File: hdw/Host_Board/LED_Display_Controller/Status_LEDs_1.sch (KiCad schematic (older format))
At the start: 5 parts

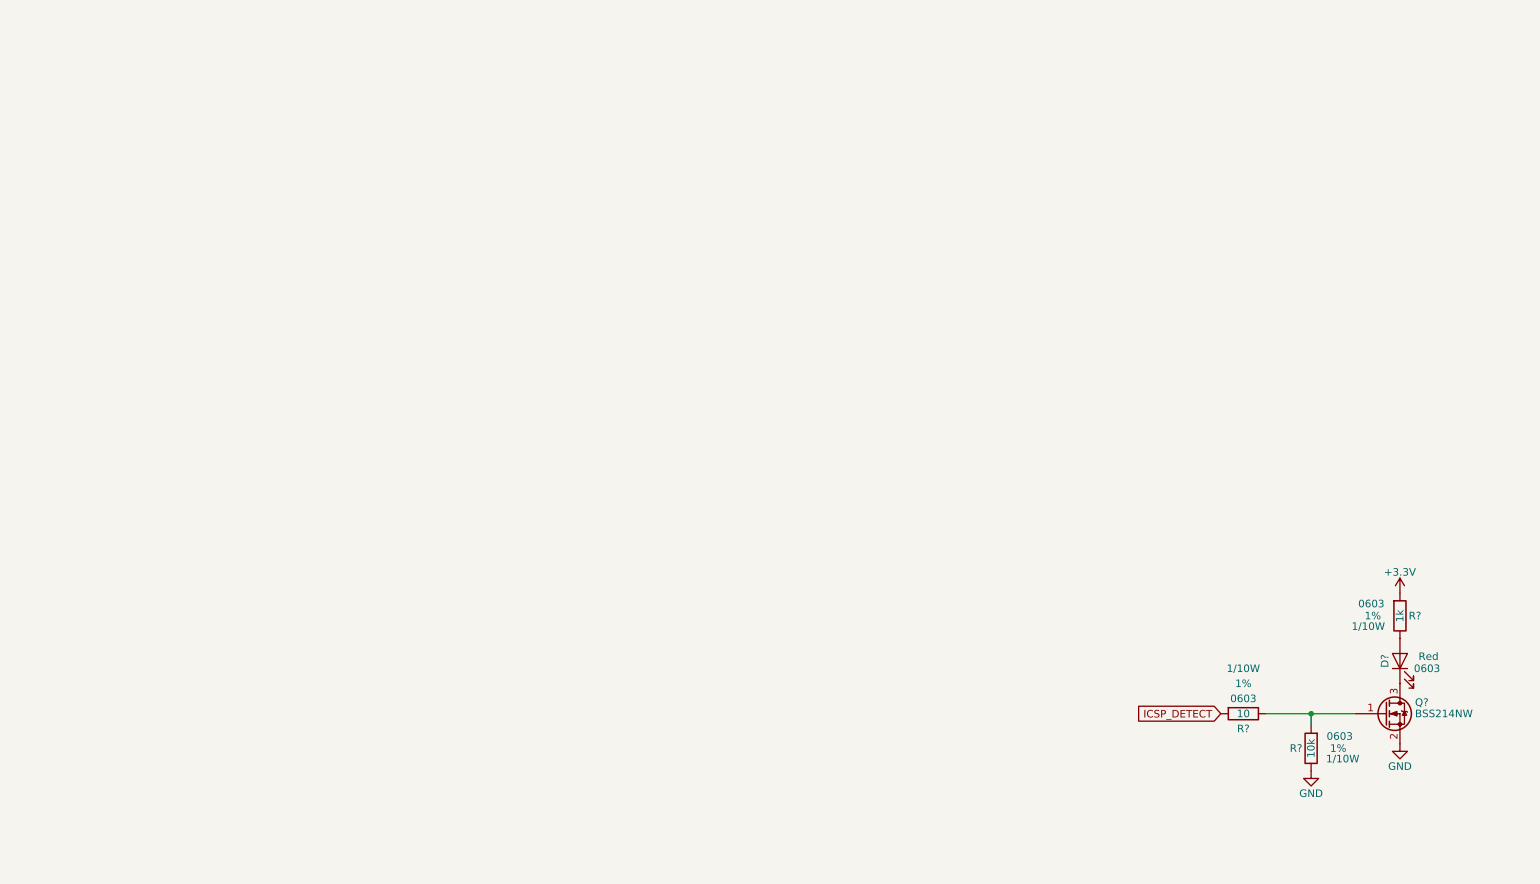
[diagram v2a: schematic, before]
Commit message: Converted to KiCad 5.0.1 project, resolved library issues, cleaned up a few sheets
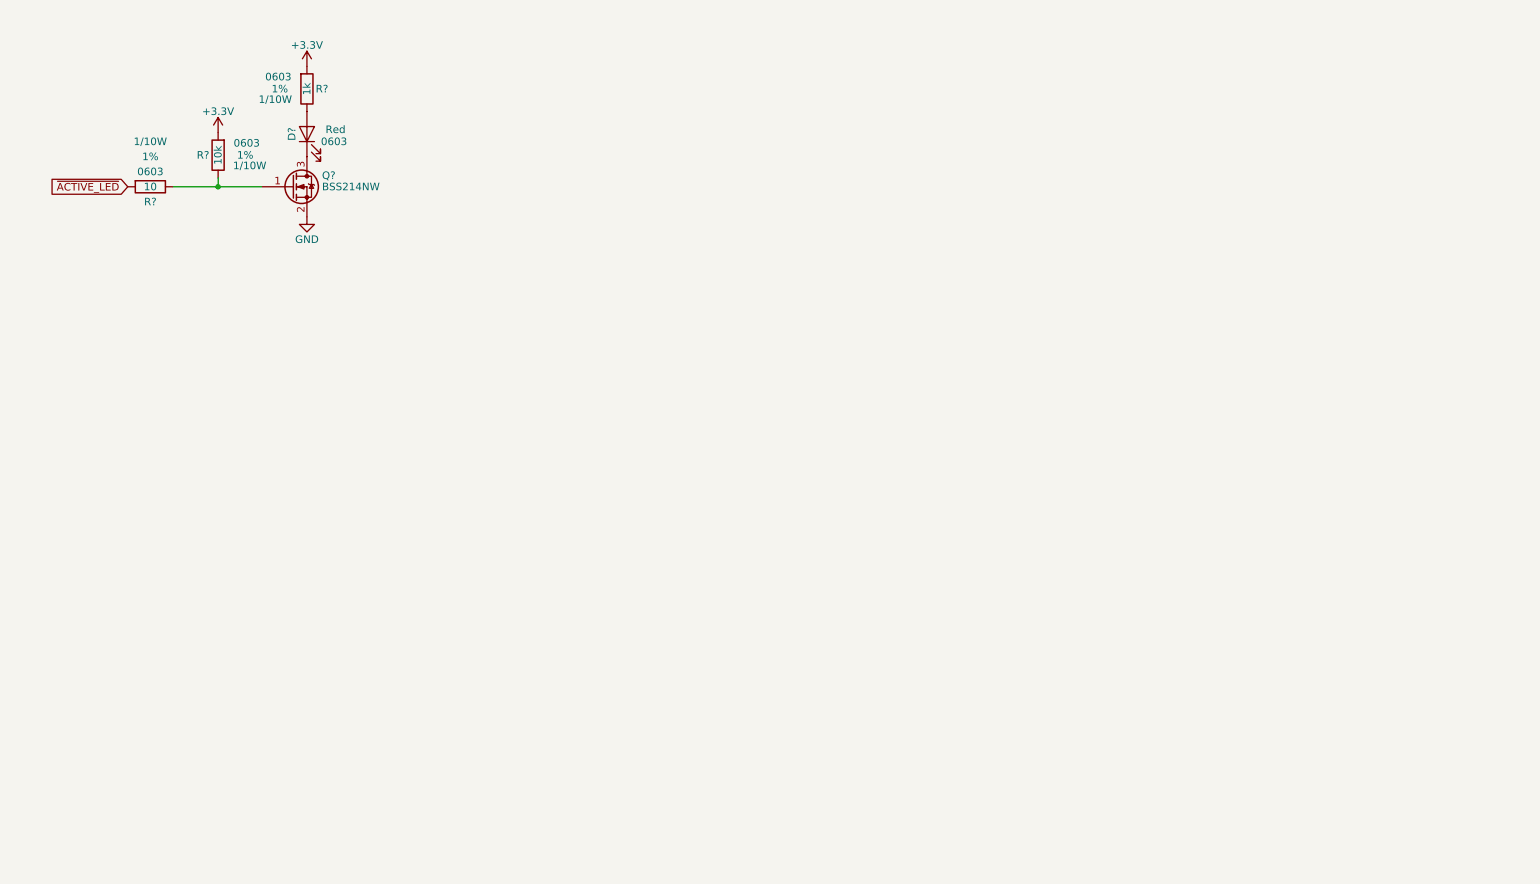
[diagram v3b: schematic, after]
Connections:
- net +3V3: now also R?.1
- net GND: no longer R?.2
- net at Q?.1 (G), R?.2: now also R?.2; no longer R?.1
- net ICSP_DETECT renamed ~ACTIVE_LED
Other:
- moved on the sheet: D?, Q?, R?
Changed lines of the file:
@@
 $Descr A 11000 8500
 encoding utf-8
-Sheet 22 25
+Sheet 21 25
 Title ""
 Date ""
@@
 L Transistor_FET:BSS214NW Q?
 U 1 1 5BC13AD2
-P 9500 5190
+P 2240 1690
 AR Path="/5BAAE16C/5BC13AD2" Ref="Q?"  Part="1"
 AR Path="/5BB844FD/5BC13AD2" Ref="Q?"  Part="1"
-F 0 "Q?" H 9700 5265 50  0000 L CNN
-F 1 "BSS214NW" H 9700 5190 50  0000 L CNN
-F 2 "Package_TO_SOT_SMD:SOT-323_SC-70" H 9700 5115 50  0001 L CIN
-F 3 "https://www.infineon.com/dgdl/Infineon-BSS214NW-DS-v02_02-en.pdf?fileId=db3a30431b3e89eb011b695aebc01bde" H 9500 5190 50  0001 L CNN
-	1    9500 5190
+F 0 "Q?" H 2440 1765 50  0000 L CNN
+F 1 "BSS214NW" H 2440 1690 50  0000 L CNN
+F 2 "Package_TO_SOT_SMD:SOT-323_SC-70" H 2440 1615 50  0001 L CIN
+F 3 "https://www.infineon.com/dgdl/Infineon-BSS214NW-DS-v02_02-en.pdf?fileId=db3a30431b3e89eb011b695aebc01bde" H 2240 1690 50  0001 L CNN
+	1    2240 1690
 	1    0    0    -1
 $EndComp
@@
 L power:GND #PWR?
 U 1 1 5BC13AD9
-P 9600 5390
-F 0 "#PWR?" H 9600 5140 50  0001 C CNN
-F 1 "GND" H 9600 5240 50  0000 C CNN
-F 2 "" H 9600 5390 50  0001 C CNN
-F 3 "" H 9600 5390 50  0001 C CNN
-	1    9600 5390
+P 2340 1890
+F 0 "#PWR?" H 2340 1640 50  0001 C CNN
+F 1 "GND" H 2340 1740 50  0000 C CNN
+F 2 "" H 2340 1890 50  0001 C CNN
+F 3 "" H 2340 1890 50  0001 C CNN
+	1    2340 1890
 	1    0    0    -1
 $EndComp
@@
 L Device:LED D?
 U 1 1 5BC13AE0
-P 9600 4840
-F 0 "D?" H 9600 4940 50  0000 C CNN
-F 1 "Red" V 9630 4650 50  0000 C CNN
-F 2 "" H 9600 4840 50  0001 C CNN
-F 3 "~" H 9600 4840 50  0001 C CNN
-F 4 "0603" V 9550 4660 50  0000 C CNN "foot"
-	1    9600 4840
+P 2340 1340
+F 0 "D?" H 2340 1440 50  0000 C CNN
+F 1 "Red" V 2370 1150 50  0000 C CNN
+F 2 "" H 2340 1340 50  0001 C CNN
+F 3 "~" H 2340 1340 50  0001 C CNN
+F 4 "0603" V 2290 1160 50  0000 C CNN "foot"
+	1    2340 1340
 	0    -1   -1   0
 $EndComp
@@
 L LED_Display_Local_Library:R_Custom R?
 U 1 1 5BC13AEB
-P 9600 4540
+P 2340 1040
 AR Path="/5BAAE1F3/5BC13AEB" Ref="R?"  Part="1"
 AR Path="/5BAAE1DC/5BC13AEB" Ref="R?"  Part="1"
 AR Path="/5BAAE16C/5BC13AEB" Ref="R?"  Part="1"
 AR Path="/5BB844FD/5BC13AEB" Ref="R?"  Part="1"
-F 0 "R?" H 9500 4540 50  0000 C CNN
-F 1 "1k" V 9600 4540 50  0000 C CNN
-F 2 "" H 9600 4540 50  0001 C CNN
-F 3 "" H 9600 4540 50  0001 C CNN
-F 4 "0603" H 9790 4620 50  0000 C CNN "display_footprint"
-F 5 "1%" H 9780 4540 50  0000 C CNN "Tolerance"
-F 6 "1/10W" H 9810 4470 50  0000 C CNN "Wattage"
-F 7 "PN" H 9900 4940 60  0001 C CNN "Digi-Key PN"
-	1    9600 4540
+F 0 "R?" H 2240 1040 50  0000 C CNN
+F 1 "1k" V 2340 1040 50  0000 C CNN
+F 2 "" H 2340 1040 50  0001 C CNN
+F 3 "" H 2340 1040 50  0001 C CNN
+F 4 "0603" H 2530 1120 50  0000 C CNN "display_footprint"
+F 5 "1%" H 2520 1040 50  0000 C CNN "Tolerance"
+F 6 "1/10W" H 2550 970 50  0000 C CNN "Wattage"
+F 7 "PN" H 2640 1440 60  0001 C CNN "Digi-Key PN"
+	1    2340 1040
 	-1   0    0    -1
 $EndComp
@@
 L LED_Display_Local_Library:R_Custom R?
 U 1 1 5BC13AF6
-P 8560 5190
-F 0 "R?" V 8460 5190 50  0000 C CNN
-F 1 "10" V 8560 5190 50  0000 C CNN
-F 2 "" H 8560 5190 50  0001 C CNN
-F 3 "" H 8560 5190 50  0001 C CNN
-F 4 "0603" V 8660 5190 50  0000 C CNN "display_footprint"
-F 5 "1%" V 8760 5190 50  0000 C CNN "Tolerance"
-F 6 "1/10W" V 8860 5190 50  0000 C CNN "Wattage"
-F 7 "PN" H 8860 5590 60  0001 C CNN "Digi-Key PN"
-	1    8560 5190
+P 1300 1690
+F 0 "R?" V 1200 1690 50  0000 C CNN
+F 1 "10" V 1300 1690 50  0000 C CNN
+F 2 "" H 1300 1690 50  0001 C CNN
+F 3 "" H 1300 1690 50  0001 C CNN
+F 4 "0603" V 1400 1690 50  0000 C CNN "display_footprint"
+F 5 "1%" V 1500 1690 50  0000 C CNN "Tolerance"
+F 6 "1/10W" V 1600 1690 50  0000 C CNN "Wattage"
+F 7 "PN" H 1600 2090 60  0001 C CNN "Digi-Key PN"
+	1    1300 1690
 	0    -1   -1   0
 $EndComp
-Text GLabel 8410 5190 0    50   Input ~ 0
-ICSP_DETECT
 $Comp
 L LED_Display_Local_Library:R_Custom R?
 U 1 1 5BC13B02
-P 9010 5420
+P 1750 1480
 AR Path="/5BAAE1F3/5BC13B02" Ref="R?"  Part="1"
 AR Path="/5BAAE1DC/5BC13B02" Ref="R?"  Part="1"
 AR Path="/5BAAE16C/5BC13B02" Ref="R?"  Part="1"
 AR Path="/5BB844FD/5BC13B02" Ref="R?"  Part="1"
-F 0 "R?" H 8910 5420 50  0000 C CNN
-F 1 "10k" V 9010 5420 50  0000 C CNN
-F 2 "" H 9010 5420 50  0001 C CNN
-F 3 "" H 9010 5420 50  0001 C CNN
-F 4 "0603" H 9200 5500 50  0000 C CNN "display_footprint"
-F 5 "1%" H 9190 5420 50  0000 C CNN "Tolerance"
-F 6 "1/10W" H 9220 5350 50  0000 C CNN "Wattage"
-F 7 "PN" H 9310 5820 60  0001 C CNN "Digi-Key PN"
-	1    9010 5420
-	1    0    0    -1
-$EndComp
-$Comp
-L power:GND #PWR?
-U 1 1 5BC13B09
-P 9010 5570
-F 0 "#PWR?" H 9010 5320 50  0001 C CNN
-F 1 "GND" H 9010 5420 50  0000 C CNN
-F 2 "" H 9010 5570 50  0001 C CNN
-F 3 "" H 9010 5570 50  0001 C CNN
-	1    9010 5570
+F 0 "R?" H 1650 1480 50  0000 C CNN
+F 1 "10k" V 1750 1480 50  0000 C CNN
+F 2 "" H 1750 1480 50  0001 C CNN
+F 3 "" H 1750 1480 50  0001 C CNN
+F 4 "0603" H 1940 1560 50  0000 C CNN "display_footprint"
+F 5 "1%" H 1930 1480 50  0000 C CNN "Tolerance"
+F 6 "1/10W" H 1960 1410 50  0000 C CNN "Wattage"
+F 7 "PN" H 2050 1880 60  0001 C CNN "Digi-Key PN"
+	1    1750 1480
 	1    0    0    -1
 $EndComp
@@
 L power:+3.3V #PWR?
 U 1 1 5BC13B0F
-P 9600 4390
-F 0 "#PWR?" H 9600 4240 50  0001 C CNN
-F 1 "+3.3V" H 9600 4530 50  0000 C CNN
-F 2 "" H 9600 4390 50  0001 C CNN
-F 3 "" H 9600 4390 50  0001 C CNN
-	1    9600 4390
+P 2340 890
+F 0 "#PWR?" H 2340 740 50  0001 C CNN
+F 1 "+3.3V" H 2340 1030 50  0000 C CNN
+F 2 "" H 2340 890 50  0001 C CNN
+F 3 "" H 2340 890 50  0001 C CNN
+	1    2340 890
 	1    0    0    -1
 $EndComp
 Wire Wire Line
-	9300 5190 9010 5190
+	1450 1690 1750 1690
+$Comp
+L power:+3.3V #PWR?
+U 1 1 5BE12615
+P 1750 1330
+F 0 "#PWR?" H 1750 1180 50  0001 C CNN
+F 1 "+3.3V" H 1750 1470 50  0000 C CNN
+F 2 "" H 1750 1330 50  0001 C CNN
+F 3 "" H 1750 1330 50  0001 C CNN
+	1    1750 1330
+	1    0    0    -1
+$EndComp
 Wire Wire Line
-	9010 5270 9010 5190
-Connection ~ 9010 5190
+	1750 1630 1750 1690
+Connection ~ 1750 1690
 Wire Wire Line
-	9010 5190 8710 5190
+	1750 1690 2040 1690
+Text GLabel 1150 1690 0    50   Input ~ 0
+~ACTIVE_LED
 $EndSCHEMATC

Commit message: Added a few pages and edits
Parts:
- removed Q?: BSS214NW, Package_TO_SOT_SMD:SOT-323_SC-70, symbol Transistor_FET:BSS214NW
- removed R?: 10, symbol LED_Display_Local_Library:R_Custom
- added C? (x6): 0.1uF, symbol LED_Display_Local_Library:C_Custom
- added D? (x4): Red, symbol Device:LED
- added D?: Green, symbol Device:LED
- added R? (x5): 1k, symbol LED_Display_Local_Library:R_Custom
- added R? (x5): 10k, symbol LED_Display_Local_Library:R_Custom
- added U? (x6): 74LVC1G06, TO_SOT_Packages_SMD:SOT-353_SC-70-5, symbol LED_Display_Local_Library:74LVC1G06_Power
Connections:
- net +3V3: now also C?.1, C?.1, C?.1, C?.1, C?.1, C?.1, R?.1, R?.1, R?.1, R?.1, R?.1, U?.5 (VCC), U?.5 (VCC), U?.5 (VCC), U?.5 (VCC), U?.5 (VCC), U?.5 (VCC)
- net GND: now also C?.2, C?.2, C?.2, C?.2, C?.2, C?.2, R?.2, R?.2, R?.2, R?.2, R?.2, U?.3 (GND), U?.3 (GND), U?.3 (GND), U?.3 (GND), U?.3 (GND), U?.3 (GND)
- net ~ACTIVE_LED: now also R?.2, U?.2
- net at D?.1 (K): now also U?.4
- new net: D?.1 (K), U?.4 (x5)
- new net: D?.2 (A), R?.2 (x5)
- new net EBI_Error_LED: R?.1, U?.2
- new net Panel_Enable_LED: R?.1, U?.2
- new net SPI_Error_LED: R?.1, U?.2
- new net USB_Error_LED: R?.1, U?.2
- new net WIFI_Error_LED: R?.1, U?.2
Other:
- moved on the sheet: D?, R?

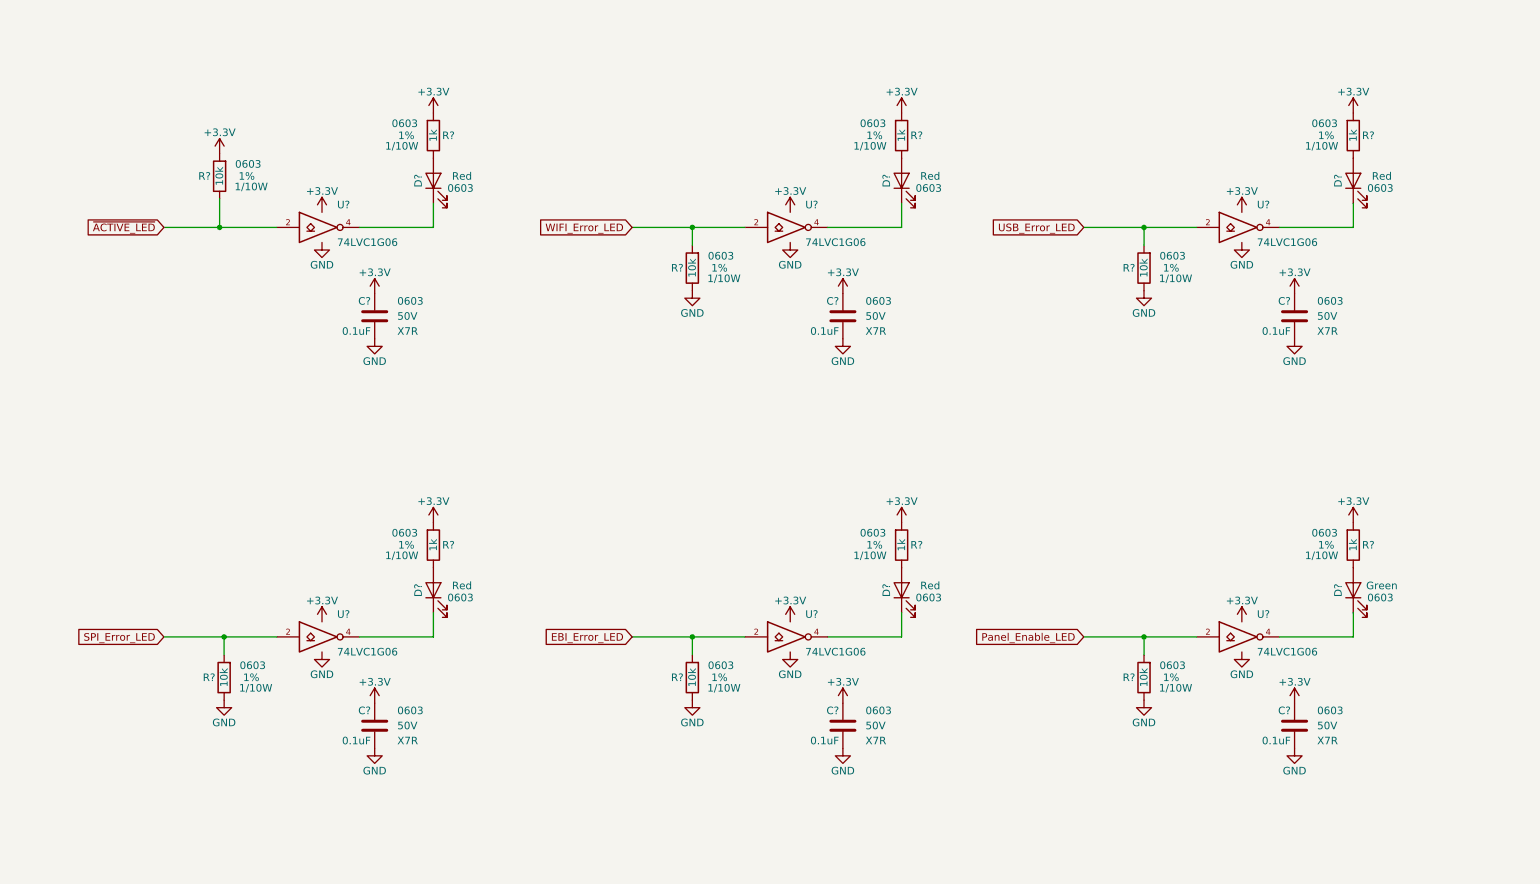
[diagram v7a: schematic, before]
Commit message: Added titles and MU logo to each sheet
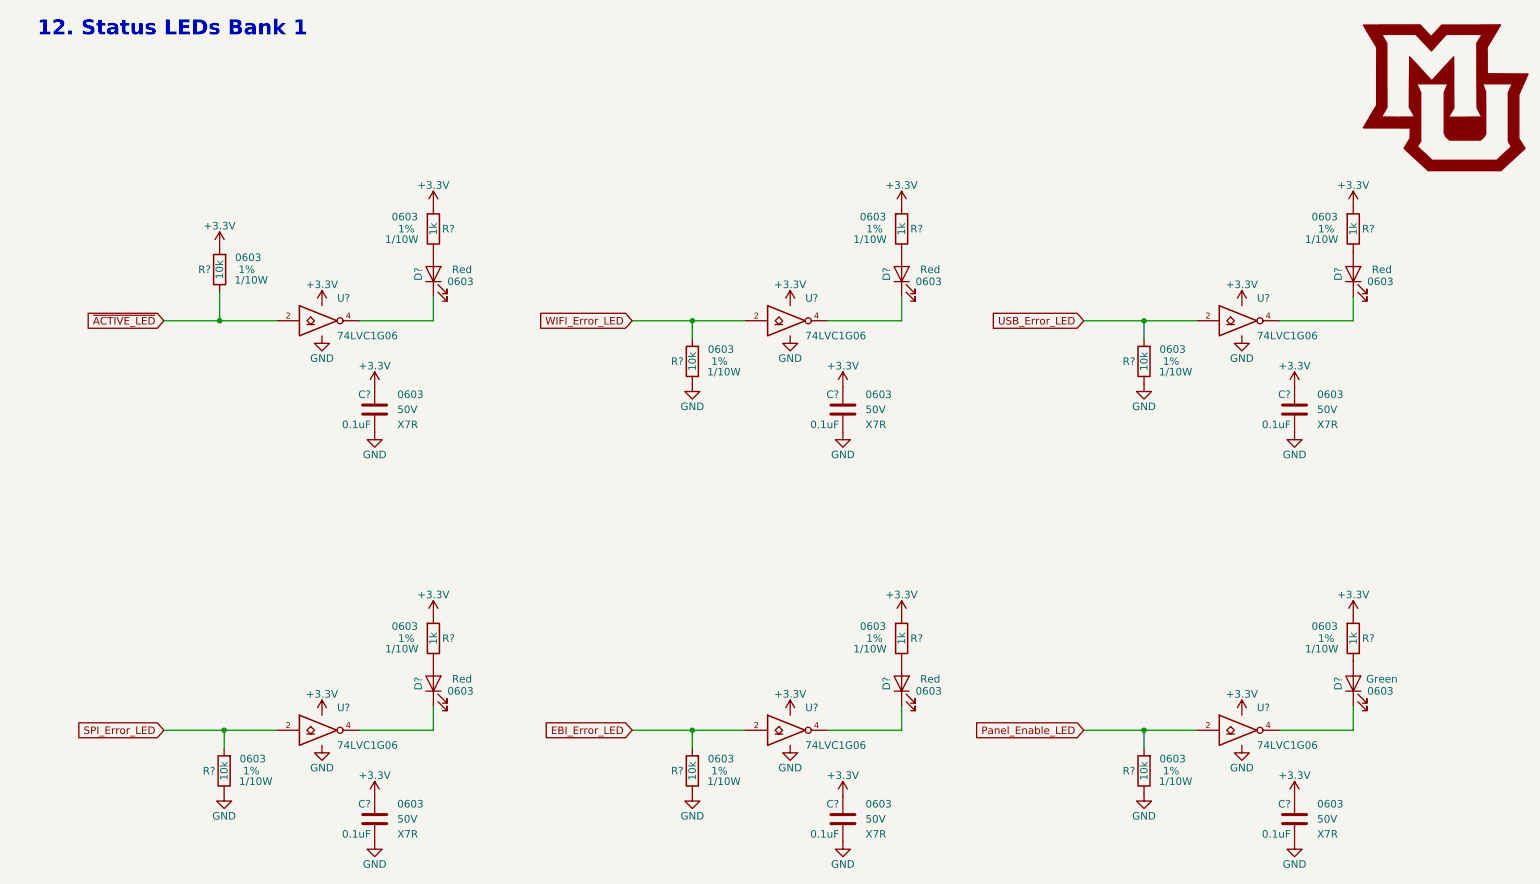
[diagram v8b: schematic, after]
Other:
- note added: "12. Status LEDs Bank 1"
- moved on the sheet: C?, D?, R?, U?
